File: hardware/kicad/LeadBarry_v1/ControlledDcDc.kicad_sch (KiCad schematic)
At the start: 7 parts, among them Q5 2N7002, U4 XL6019E1 Module

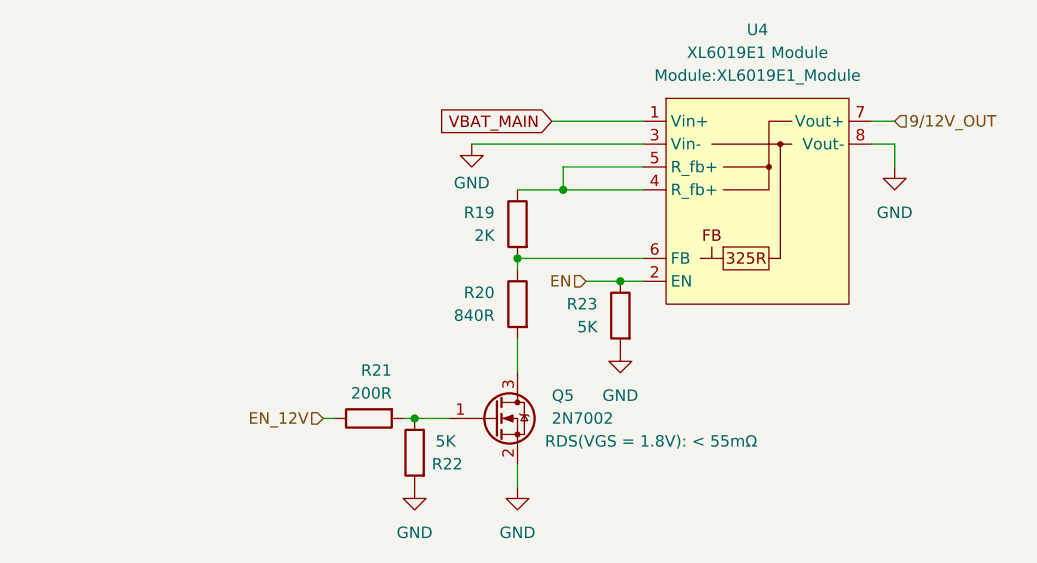
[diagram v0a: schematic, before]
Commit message: fix: implemented regulated voltage schematic
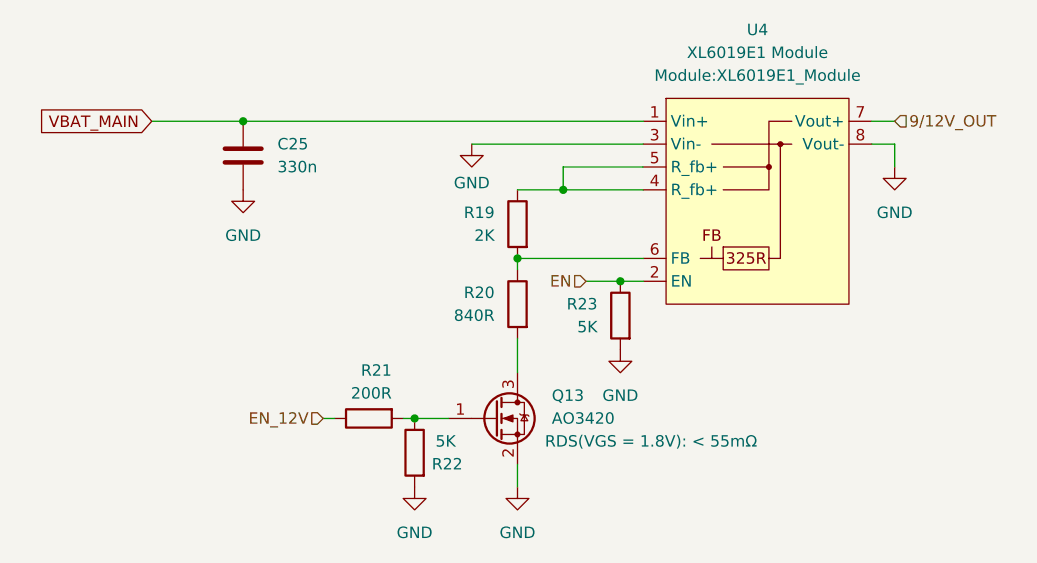
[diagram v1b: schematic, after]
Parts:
- added C25: 330n, Capacitor_SMD:C_1206_3216Metric_Pad1.33x1.80mm_HandSolder, symbol Device:C
- Q13: renamed from Q5; value 2N7002 -> AO3420
- R19, R20, R21, R22, R23: footprint Resistor_THT:R_Axial_DIN0207_L6.3mm_D2.5mm_P10.16mm_Horizontal -> Resistor_SMD:R_0805_2012Metric_Pad1.20x1.40mm_HandSolder
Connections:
- net GND: now also C25.2
- net VBAT_MAIN: now also C25.1
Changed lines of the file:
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@@
+	)
+	(junction
+		(at 102.87 85.09)
+		(diameter 0)
+		(color 0 0 0 0)
 	)
 	(junction
@@
 	(wire
 		(pts
+			(xy 102.87 85.09) (xy 147.32 85.09)
+		)
+		(stroke
+			(width 0)
+			(type default)
+		)
+	)
+	(wire
+		(pts
 			(xy 133.35 100.33) (xy 147.32 100.33)
 		)
@@
 	(wire
 		(pts
-			(xy 137.16 85.09) (xy 147.32 85.09)
+			(xy 92.71 85.09) (xy 102.87 85.09)
 		)
 		(stroke
@@
 	(global_label "VBAT_MAIN"
 		(shape input)
-		(at 137.16 85.09 180)
+		(at 92.71 85.09 180)
 		(fields_autoplaced yes)
 		(effects
@@
 		)
 		(property "Intersheetrefs" "${INTERSHEET_REFS}"
-			(at 124.3171 85.09 0)
+			(at 79.8671 85.09 0)
 			(effects
 				(font
@@
 			)
 		)
-		(property "Footprint" "Resistor_THT:R_Axial_DIN0207_L6.3mm_D2.5mm_P10.16mm_Horizontal"
+		(property "Footprint" "Resistor_SMD:R_0805_2012Metric_Pad1.20x1.40mm_HandSolder"
 			(at 135.128 105.41 90)
 			(effects
@@
 		(instances
 			(project "LeadBarry_v1"
+				(path "/20771d85-0a47-48d4-b39f-5d01020408af/1a5c9110-8742-4ce5-925b-2759184d3a24/a4bf1372-bbd6-4b42-a288-585c477f5e8d"
+					(reference "R50")
+					(unit 1)
+				)
 				(path "/20771d85-0a47-48d4-b39f-5d01020408af/1a5c9110-8742-4ce5-925b-2759184d3a24/eebf9a5b-85c1-451b-802d-a0649c09e85e"
 					(reference "R20")
@@
 			)
 		)
-		(property "Footprint" "Resistor_THT:R_Axial_DIN0207_L6.3mm_D2.5mm_P10.16mm_Horizontal"
+		(property "Footprint" "Resistor_SMD:R_0805_2012Metric_Pad1.20x1.40mm_HandSolder"
 			(at 146.558 106.68 90)
 			(effects
@@
 		(instances
 			(project "LeadBarry_v1"
+				(path "/20771d85-0a47-48d4-b39f-5d01020408af/1a5c9110-8742-4ce5-925b-2759184d3a24/a4bf1372-bbd6-4b42-a288-585c477f5e8d"
+					(reference "R51")
+					(unit 1)
+				)
 				(path "/20771d85-0a47-48d4-b39f-5d01020408af/1a5c9110-8742-4ce5-925b-2759184d3a24/eebf9a5b-85c1-451b-802d-a0649c09e85e"
 					(reference "R23")
@@
 			)
 		)
-		(property "Footprint" "Resistor_THT:R_Axial_DIN0207_L6.3mm_D2.5mm_P10.16mm_Horizontal"
+		(property "Footprint" "Resistor_SMD:R_0805_2012Metric_Pad1.20x1.40mm_HandSolder"
 			(at 135.128 96.52 90)
 			(effects
@@
 		(instances
 			(project "LeadBarry_v1"
+				(path "/20771d85-0a47-48d4-b39f-5d01020408af/1a5c9110-8742-4ce5-925b-2759184d3a24/a4bf1372-bbd6-4b42-a288-585c477f5e8d"
+					(reference "R49")
+					(unit 1)
+				)
 				(path "/20771d85-0a47-48d4-b39f-5d01020408af/1a5c9110-8742-4ce5-925b-2759184d3a24/eebf9a5b-85c1-451b-802d-a0649c09e85e"
 					(reference "R19")
@@
 		(instances
 			(project "LeadBarry_v1"
+				(path "/20771d85-0a47-48d4-b39f-5d01020408af/1a5c9110-8742-4ce5-925b-2759184d3a24/a4bf1372-bbd6-4b42-a288-585c477f5e8d"
+					(reference "#PWR051")
+					(unit 1)
+				)
 				(path "/20771d85-0a47-48d4-b39f-5d01020408af/1a5c9110-8742-4ce5-925b-2759184d3a24/eebf9a5b-85c1-451b-802d-a0649c09e85e"
 					(reference "#PWR022")
@@
 		(dnp no)
 		(fields_autoplaced yes)
-		(property "Reference" "U4"
+		(property "Reference" "U?"
 			(at 160.02 74.93 0)
 			(effects
@@
 		)
 		(instances
-			(project ""
+			(project "LeadBarry_v1"
+				(path "/20771d85-0a47-48d4-b39f-5d01020408af/1a5c9110-8742-4ce5-925b-2759184d3a24/a4bf1372-bbd6-4b42-a288-585c477f5e8d"
+					(reference "U4")
+					(unit 1)
+				)
 				(path "/20771d85-0a47-48d4-b39f-5d01020408af/1a5c9110-8742-4ce5-925b-2759184d3a24/eebf9a5b-85c1-451b-802d-a0649c09e85e"
-					(reference "U4")
+					(reference "U?")
 					(unit 1)
 				)
@@
 			)
 		)
-		(property "Footprint" "Resistor_THT:R_Axial_DIN0207_L6.3mm_D2.5mm_P10.16mm_Horizontal"
+		(property "Footprint" "Resistor_SMD:R_0805_2012Metric_Pad1.20x1.40mm_HandSolder"
 			(at 123.698 121.92 90)
 			(effects
@@
 		(instances
 			(project "LeadBarry_v1"
+				(path "/20771d85-0a47-48d4-b39f-5d01020408af/1a5c9110-8742-4ce5-925b-2759184d3a24/a4bf1372-bbd6-4b42-a288-585c477f5e8d"
+					(reference "R48")
+					(unit 1)
+				)
 				(path "/20771d85-0a47-48d4-b39f-5d01020408af/1a5c9110-8742-4ce5-925b-2759184d3a24/eebf9a5b-85c1-451b-802d-a0649c09e85e"
 					(reference "R22")
@@
 		(instances
 			(project "LeadBarry_v1"
+				(path "/20771d85-0a47-48d4-b39f-5d01020408af/1a5c9110-8742-4ce5-925b-2759184d3a24/a4bf1372-bbd6-4b42-a288-585c477f5e8d"
+					(reference "#PWR053")
+					(unit 1)
+				)
 				(path "/20771d85-0a47-48d4-b39f-5d01020408af/1a5c9110-8742-4ce5-925b-2759184d3a24/eebf9a5b-85c1-451b-802d-a0649c09e85e"
 					(reference "#PWR020")
@@
 		(on_board yes)
 		(dnp no)
-		(property "Reference" "#PWR019"
+		(property "Reference" "#PWR?"
 			(at 128.27 93.98 0)
 			(effects
@@
 		)
 		(instances
-			(project ""
+			(project "LeadBarry_v1"
+				(path "/20771d85-0a47-48d4-b39f-5d01020408af/1a5c9110-8742-4ce5-925b-2759184d3a24/a4bf1372-bbd6-4b42-a288-585c477f5e8d"
+					(reference "#PWR052")
+					(unit 1)
+				)
 				(path "/20771d85-0a47-48d4-b39f-5d01020408af/1a5c9110-8742-4ce5-925b-2759184d3a24/eebf9a5b-85c1-451b-802d-a0649c09e85e"
-					(reference "#PWR019")
+					(reference "#PWR?")
+					(unit 1)
+				)
+			)
+		)
+	)
+	(symbol
+		(lib_id "Device:C")
+		(at 102.87 88.9 0)
+		(unit 1)
+		(exclude_from_sim no)
+		(in_bom yes)
+		(on_board yes)
+		(dnp no)
+		(fields_autoplaced yes)
+		(property "Reference" "C25"
+			(at 106.68 87.6299 0)
+			(effects
+				(font
+					(size 1.27 1.27)
+				)
+				(justify left)
+			)
+		)
+		(property "Value" "330n"
+			(at 106.68 90.1699 0)
+			(effects
+				(font
+					(size 1.27 1.27)
+				)
+				(justify left)
+			)
+		)
+		(property "Footprint" "Capacitor_SMD:C_1206_3216Metric_Pad1.33x1.80mm_HandSolder"
+			(at 103.8352 92.71 0)
+			(effects
+				(font
+					(size 1.27 1.27)
+				)
+				(hide yes)
+			)
+		)
+		(property "Datasheet" "~"
+			(at 102.87 88.9 0)
+			(effects
+				(font
+					(size 1.27 1.27)
+				)
+				(hide yes)
+			)
+		)
+		(property "Description" "Unpolarized capacitor"
+			(at 102.87 88.9 0)
+			(effects
+				(font
+					(size 1.27 1.27)
+				)
+				(hide yes)
+			)
+		)
+		(pin "2"
+		)
+		(pin "1"
+		)
+		(instances
+			(project "LeadBarry_v1"
+				(path "/20771d85-0a47-48d4-b39f-5d01020408af/1a5c9110-8742-4ce5-925b-2759184d3a24/a4bf1372-bbd6-4b42-a288-585c477f5e8d"
+					(reference "C25")
 					(unit 1)
 				)
@@
 			)
 		)
-		(property "Footprint" "Resistor_THT:R_Axial_DIN0207_L6.3mm_D2.5mm_P10.16mm_Horizontal"
+		(property "Footprint" "Resistor_SMD:R_0805_2012Metric_Pad1.20x1.40mm_HandSolder"
 			(at 116.84 116.332 90)
 			(effects
@@
 		(instances
 			(project "LeadBarry_v1"
+				(path "/20771d85-0a47-48d4-b39f-5d01020408af/1a5c9110-8742-4ce5-925b-2759184d3a24/a4bf1372-bbd6-4b42-a288-585c477f5e8d"
+					(reference "R47")
+					(unit 1)
+				)
 				(path "/20771d85-0a47-48d4-b39f-5d01020408af/1a5c9110-8742-4ce5-925b-2759184d3a24/eebf9a5b-85c1-451b-802d-a0649c09e85e"
 					(reference "R21")
@@
 		(instances
 			(project "LeadBarry_v1"
+				(path "/20771d85-0a47-48d4-b39f-5d01020408af/1a5c9110-8742-4ce5-925b-2759184d3a24/a4bf1372-bbd6-4b42-a288-585c477f5e8d"
+					(reference "#PWR054")
+					(unit 1)
+				)
 				(path "/20771d85-0a47-48d4-b39f-5d01020408af/1a5c9110-8742-4ce5-925b-2759184d3a24/eebf9a5b-85c1-451b-802d-a0649c09e85e"
 					(reference "#PWR023")
+					(unit 1)
+				)
+			)
+		)
+	)
+	(symbol
+		(lib_id "power:GND")
+		(at 102.87 92.71 0)
+		(unit 1)
+		(exclude_from_sim no)
+		(in_bom yes)
+		(on_board yes)
+		(dnp no)
+		(fields_autoplaced yes)
+		(property "Reference" "#PWR046"
+			(at 102.87 99.06 0)
+			(effects
+				(font
+					(size 1.27 1.27)
+				)
+				(hide yes)
+			)
+		)
+		(property "Value" "GND"
+			(at 102.87 97.79 0)
+			(effects
+				(font
+					(size 1.27 1.27)
+				)
+			)
+		)
+		(property "Footprint" ""
+			(at 102.87 92.71 0)
+			(effects
+				(font
+					(size 1.27 1.27)
+				)
+				(hide yes)
+			)
+		)
+		(property "Datasheet" ""
+			(at 102.87 92.71 0)
+			(effects
+				(font
+					(size 1.27 1.27)
+				)
+				(hide yes)
+			)
+		)
+		(property "Description" "Power symbol creates a global label with name \"GND\" , ground"
+			(at 102.87 92.71 0)
+			(effects
+				(font
+					(size 1.27 1.27)
+				)
+				(hide yes)
+			)
+		)
+		(pin "1"
+		)
+		(instances
+			(project "LeadBarry_v1"
+				(path "/20771d85-0a47-48d4-b39f-5d01020408af/1a5c9110-8742-4ce5-925b-2759184d3a24/a4bf1372-bbd6-4b42-a288-585c477f5e8d"
+					(reference "#PWR050")
+					(unit 1)
+				)
+				(path "/20771d85-0a47-48d4-b39f-5d01020408af/1a5c9110-8742-4ce5-925b-2759184d3a24/eebf9a5b-85c1-451b-802d-a0649c09e85e"
+					(reference "#PWR046")
 					(unit 1)
 				)
@@
 		(instances
 			(project "LeadBarry_v1"
+				(path "/20771d85-0a47-48d4-b39f-5d01020408af/1a5c9110-8742-4ce5-925b-2759184d3a24/a4bf1372-bbd6-4b42-a288-585c477f5e8d"
+					(reference "#PWR055")
+					(unit 1)
+				)
 				(path "/20771d85-0a47-48d4-b39f-5d01020408af/1a5c9110-8742-4ce5-925b-2759184d3a24/eebf9a5b-85c1-451b-802d-a0649c09e85e"
 					(reference "#PWR021")
@@
 		(on_board yes)
 		(dnp no)
-		(property "Reference" "Q5"
+		(property "Reference" "Q13"
 			(at 137.16 115.5699 0)
 			(effects
@@
 			)
 		)
-		(property "Value" "2N7002"
+		(property "Value" "AO3420"
 			(at 137.16 118.1099 0)
 			(effects
@@
 		)
 		(instances
-			(project ""
-				(path "/20771d85-0a47-48d4-b39f-5d01020408af/1a5c9110-8742-4ce5-925b-2759184d3a24/eebf9a5b-85c1-451b-802d-a0649c09e85e"
-					(reference "Q5")
-					(unit 1)
-				)
+			(project "LeadBarry_v1"
+				(path "/20771d85-0a47-48d4-b39f-5d01020408af/1a5c9110-8742-4ce5-925b-2759184d3a24/a4bf1372-bbd6-4b42-a288-585c477f5e8d"
+					(reference "Q13")
+					(unit 1)
+				)
